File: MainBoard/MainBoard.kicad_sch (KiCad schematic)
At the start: 24 parts, among them J1 1761681-3, U1 TL072CP

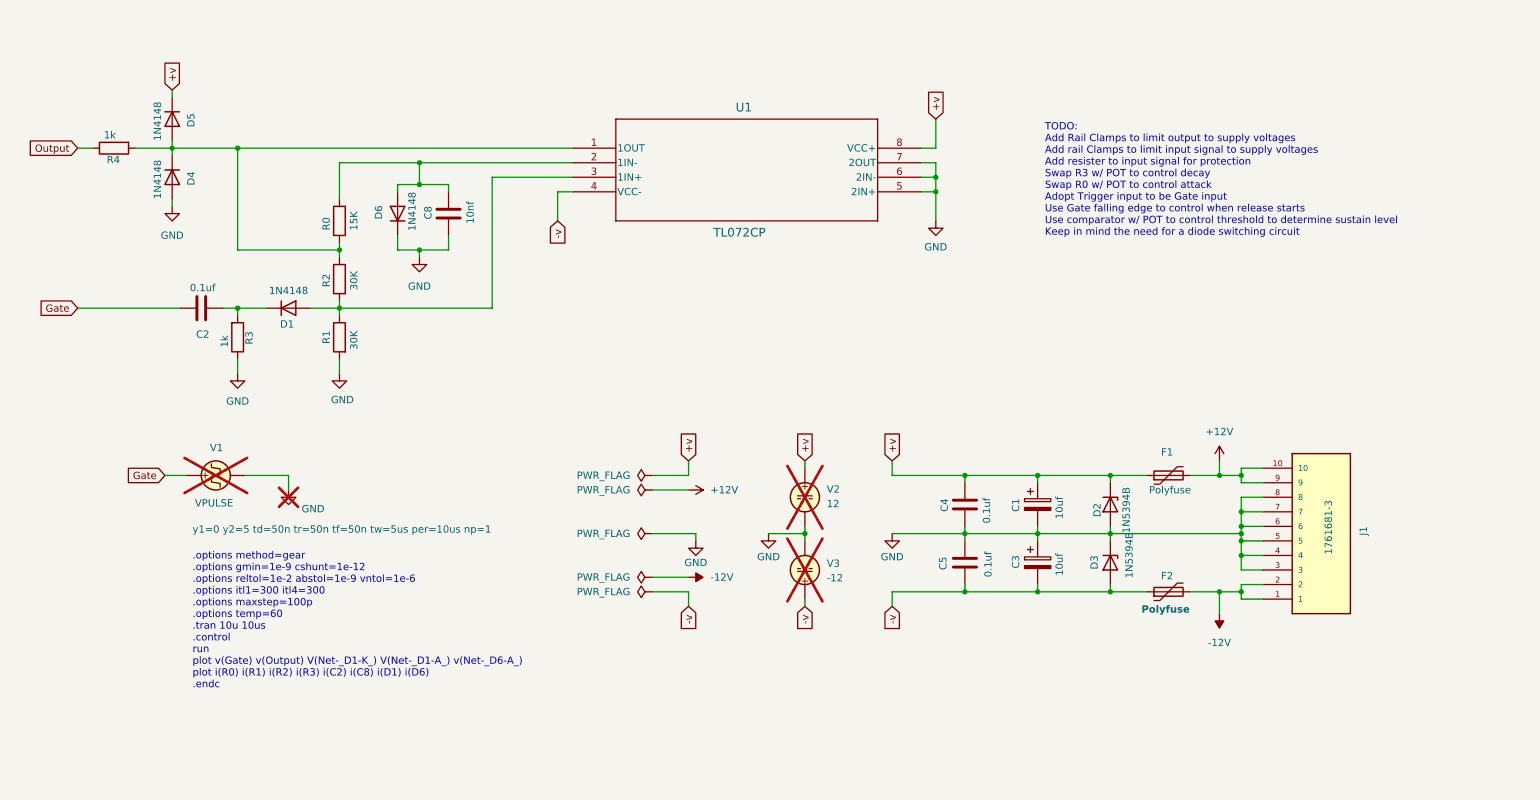
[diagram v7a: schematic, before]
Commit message: added buffered input, flipped schematic horizontally so inputs on left and output on right
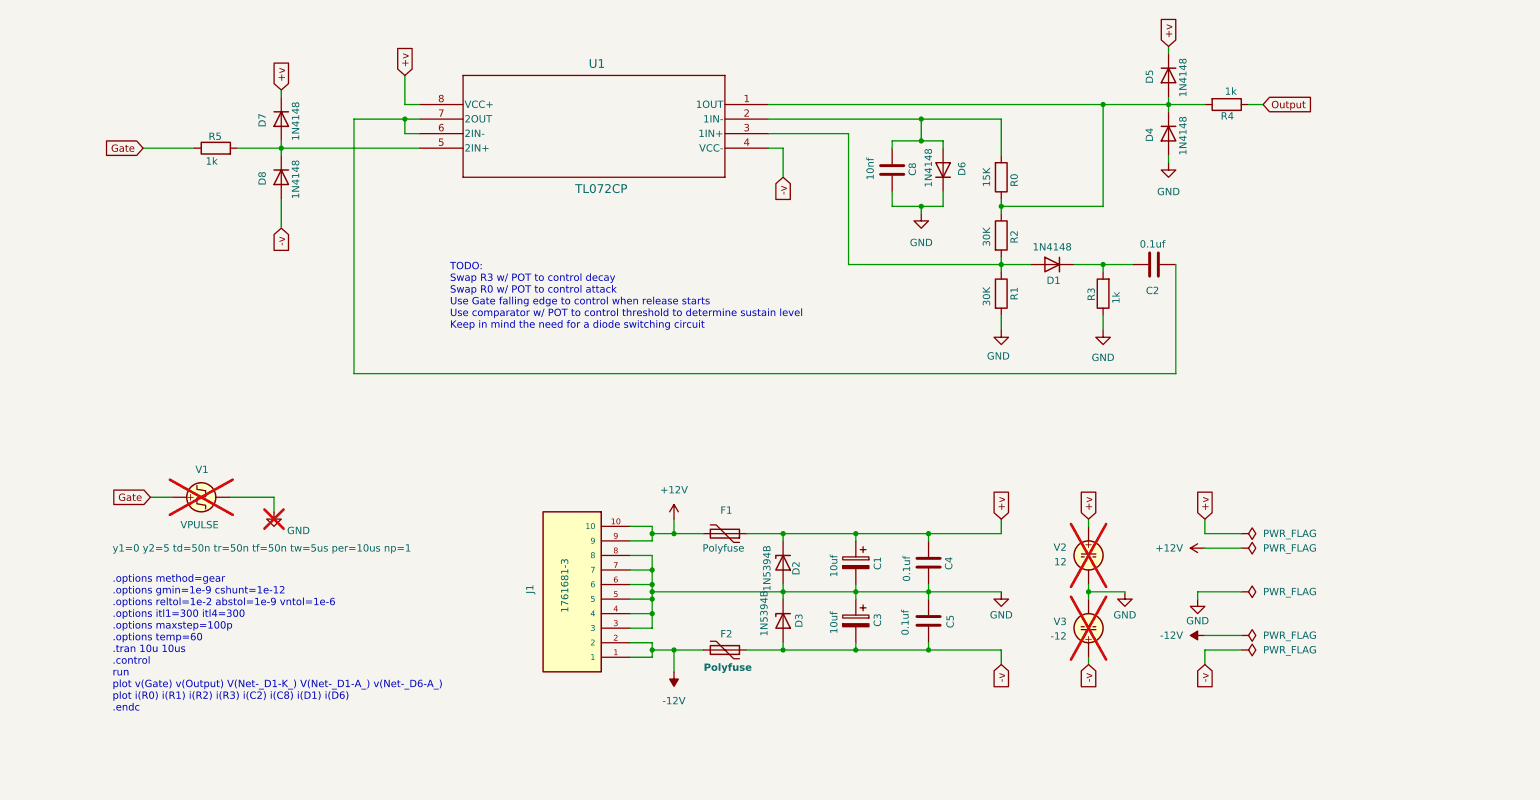
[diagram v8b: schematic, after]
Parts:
- added D7, D8: 1N4148, symbol Device:D
- added R5: 1k, symbol Device:R
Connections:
- net +v: now also D7.1 (K)
- net -v: now also D8.2 (A)
- net GND: no longer U1.5 (2IN+), U1.6 (2IN-), U1.7 (2OUT)
- net Gate: now also R5.1; no longer C2.2
- new net: D7.2 (A), D8.1 (K), R5.2, U1.5 (2IN+)
- new net: C2.2, U1.6 (2IN-), U1.7 (2OUT)
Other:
- note added: "TODO: Swap R3 w/ POT to control decay Swap R0 w/ POT to control attack Use Gate falling edge to control when release starts Use comparator w/ POT to control threshold to determine sustain level Keep in mind the need for a diode switching circuit"
- note removed: "TODO: Add Rail Clamps to limit output to supply voltages Add rail Clamps to limit input signal to supply voltages Add resister to input signal for protection Swap R3 w/ POT to control decay Swap R0 w/ POT to control attack Adopt Trigger input to be Gate input Use Gate falling edge to control when release starts Use comparator w/ POT to control threshold to determine sustain level Keep in mind the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"
- moved on the sheet: C1, C2, C3, C4, C5, C8, D1, D2, D3, D4, D5, D6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
